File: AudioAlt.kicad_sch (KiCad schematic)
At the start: 37 parts, among them J6 SJ-3524-SMT-TR, Q5 DMP3068L-7, U6 WM8731SEDS

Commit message: Board stuffing, new audio on board
Added new Audio IC to PCB.
Started moving everything into a estimated board size, AKA restricted area. Things seem REALL TIGHT. There's not enough space, I think I'll have to change resistor footprints
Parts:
- removed R73, R74: 47kΩ, Resistor_SMD:R_0805_2012Metric, symbol Device:R_Small_US
- added R10, R11: 10kΩ, Resistor_SMD:R_0603_1608Metric_Pad0.98x0.95mm_HandSolder, symbol Device:R_Small_US
- R3, R61, R62, R63, R64, R65, R66, R67, R68, R69, R70, R71, R72, R75, R76: footprint Resistor_SMD:R_0805_2012Metric -> Resistor_SMD:R_0603_1608Metric_Pad0.98x0.95mm_HandSolder
- TP12, TP13, TP14, TP15, TP16: footprint (none) -> TestPoint:TestPoint_Pad_1.5x1.5mm
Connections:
- net A2_MCLK: now also R10.1
- net A2_TSW: now also R11.1
- net GND: now also R10.2, R11.2
- net A2_CSB_n: no longer names the net of U6.22 (~{CSB})
- net A2_CSB_n: now also R65.1; no longer R64.1
- net A2_MODE: no longer names the net of U6.21 (MODE)
- net A2_MODE: now also R64.1; no longer R65.1

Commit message: Compacting part 1
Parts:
- removed R70: 0Ω, Resistor_SMD:R_0603_1608Metric_Pad0.98x0.95mm_HandSolder, symbol Device:R_Small_US
- renumbered dC6 to C70, dC7 to C71, dC8 to C72, dC9 to C73, dC36 to C74, dC37 to C75, dC34 to C76, dC35 to C77, dC12 to C78, dC14 to C79, C8 to C80, C9 to C81, J6 to J70, Q5 to Q70, R61 to R70, R3 to R71, R65 to R72, R64 to R73, R76 to R74, R72 to R75, R71 to R76, R10 to R77, R75 to R78, R62 to R79, R63 to R80, R67 to R81, R68 to R82, R69 to R83, R66 to R84, R11 to R85, TP16 to TP70, TP15 to TP71, TP12 to TP72, TP13 to TP73, U6 to U70
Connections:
- net A2_TSW: now also J70.TN
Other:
- moved on the sheet: R85

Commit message: Ground Stitching, PMOS 0-Res Moved,
DRC should be near cleared. Might want to reconsider mapping some pin functions? SD card detect line, also battery checker (making use of comparator). Also, double check if audio IC microphone pins (and ADC) are supposed to be pulled to VMID
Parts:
- TP14, TP70, TP71, TP72, TP73: footprint TestPoint:TestPoint_Pad_1.5x1.5mm -> footprints:TestPoint_Pad_1.5x1.5mm
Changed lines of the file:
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@@
 			)
 		)
-		(property "Footprint" "TestPoint:TestPoint_Pad_1.5x1.5mm"
+		(property "Footprint" "footprints:TestPoint_Pad_1.5x1.5mm"
 			(at 171.45 110.49 0)
 			(effects
@@
 			)
 		)
-		(property "Footprint" "TestPoint:TestPoint_Pad_1.5x1.5mm"
+		(property "Footprint" "footprints:TestPoint_Pad_1.5x1.5mm"
 			(at 135.89 121.92 0)
 			(effects
@@
 			)
 		)
-		(property "Footprint" "TestPoint:TestPoint_Pad_1.5x1.5mm"
+		(property "Footprint" "footprints:TestPoint_Pad_1.5x1.5mm"
 			(at 171.45 107.95 0)
 			(effects
@@
 			)
 		)
-		(property "Footprint" "TestPoint:TestPoint_Pad_1.5x1.5mm"
+		(property "Footprint" "footprints:TestPoint_Pad_1.5x1.5mm"
 			(at 124.46 116.84 0)
 			(effects
@@
 			)
 		)
-		(property "Footprint" "TestPoint:TestPoint_Pad_1.5x1.5mm"
+		(property "Footprint" "footprints:TestPoint_Pad_1.5x1.5mm"
 			(at 110.49 85.09 0)
 			(effects

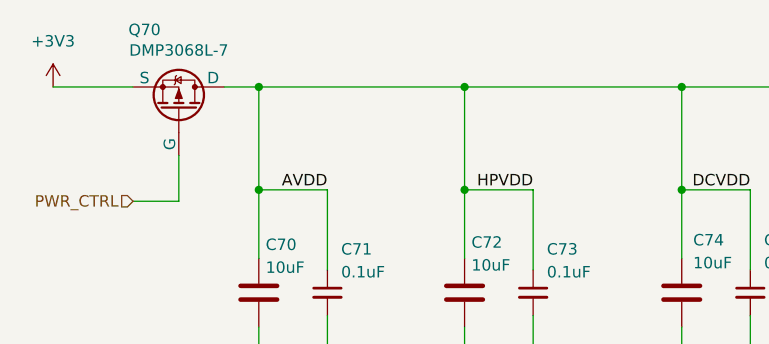
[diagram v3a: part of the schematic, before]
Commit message: UNFINISHED: Rerouted Traces, new LEDs, replaced components
Removed charging status and power source signals from MCU and gave them their own LEDs. Added analog battery voltage and card detect as replacement. Also found out not all components are in stock... troubling to find replacements :( should have done this during schematic
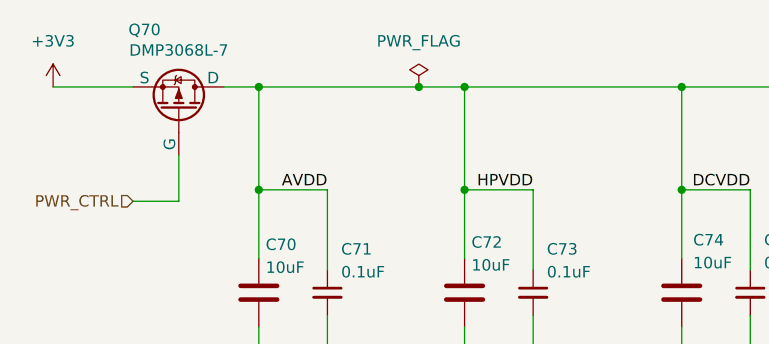
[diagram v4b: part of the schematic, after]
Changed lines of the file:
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@@
+	)
+	(junction
+		(at 60.96 21.59)
+		(diameter 0)
+		(color 0 0 0 0)
 	)
 	(junction
@@
 	(wire
 		(pts
-			(xy 43.18 21.59) (xy 66.04 21.59)
+			(xy 43.18 21.59) (xy 60.96 21.59)
 		)
 		(stroke
@@
 		(pts
 			(xy 124.46 92.71) (xy 135.89 92.71)
+		)
+		(stroke
+			(width 0)
+			(type default)
+		)
+	)
+	(wire
+		(pts
+			(xy 60.96 21.59) (xy 66.04 21.59)
 		)
 		(stroke
@@
 					(unit 1)
 				)
+			)
+		)
+	)
+	(symbol
+		(lib_id "power:PWR_FLAG")
+		(at 60.96 21.59 0)
+		(unit 1)
+		(exclude_from_sim no)
+		(in_bom yes)
+		(on_board yes)
+		(dnp no)
+		(fields_autoplaced yes)
+		(property "Reference" "#FLG04"
+			(at 60.96 19.685 0)
+			(effects
+				(font
+					(size 1.27 1.27)
+				)
+				(hide yes)
+			)
+		)
+		(property "Value" "PWR_FLAG"
+			(at 60.96 16.51 0)
+			(effects
+				(font
+					(size 1.27 1.27)
+				)
+			)
+		)
+		(property "Footprint" ""
+			(at 60.96 21.59 0)
+			(effects
+				(font
+					(size 1.27 1.27)
+				)
+				(hide yes)
+			)
+		)
+		(property "Datasheet" "~"
+			(at 60.96 21.59 0)
+			(effects
+				(font
+					(size 1.27 1.27)
+				)
+				(hide yes)
+			)
+		)
+		(property "Description" "Special symbol for telling ERC where power comes from"
+			(at 60.96 21.59 0)
+			(effects
+				(font
+					(size 1.27 1.27)
+				)
+				(hide yes)
+			)
+		)
+		(pin "1"
+		)
+		(instances
+			(project ""
+				(path "/5c19345b-3707-4c90-b593-78a9c3e56866/f44db6d7-c45e-4150-a777-8c6c189bba1b"
+					(reference "#FLG04")
+					(unit 1)
+				)
